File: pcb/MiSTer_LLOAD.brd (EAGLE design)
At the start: 100 x 80 mm, 22 parts, among them K1 692121030100

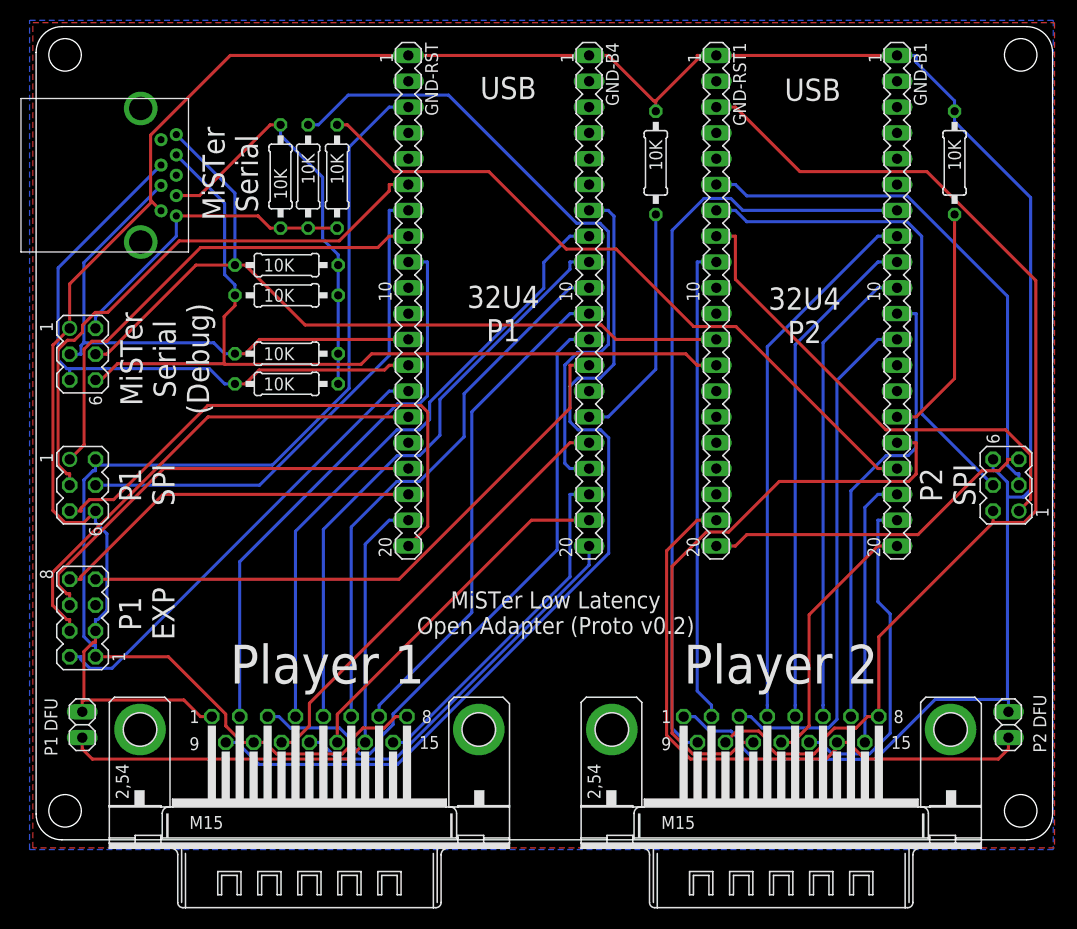
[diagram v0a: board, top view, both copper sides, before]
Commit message: Proto v0.3 PCB - It does not rely on Serial IO VCC anymore
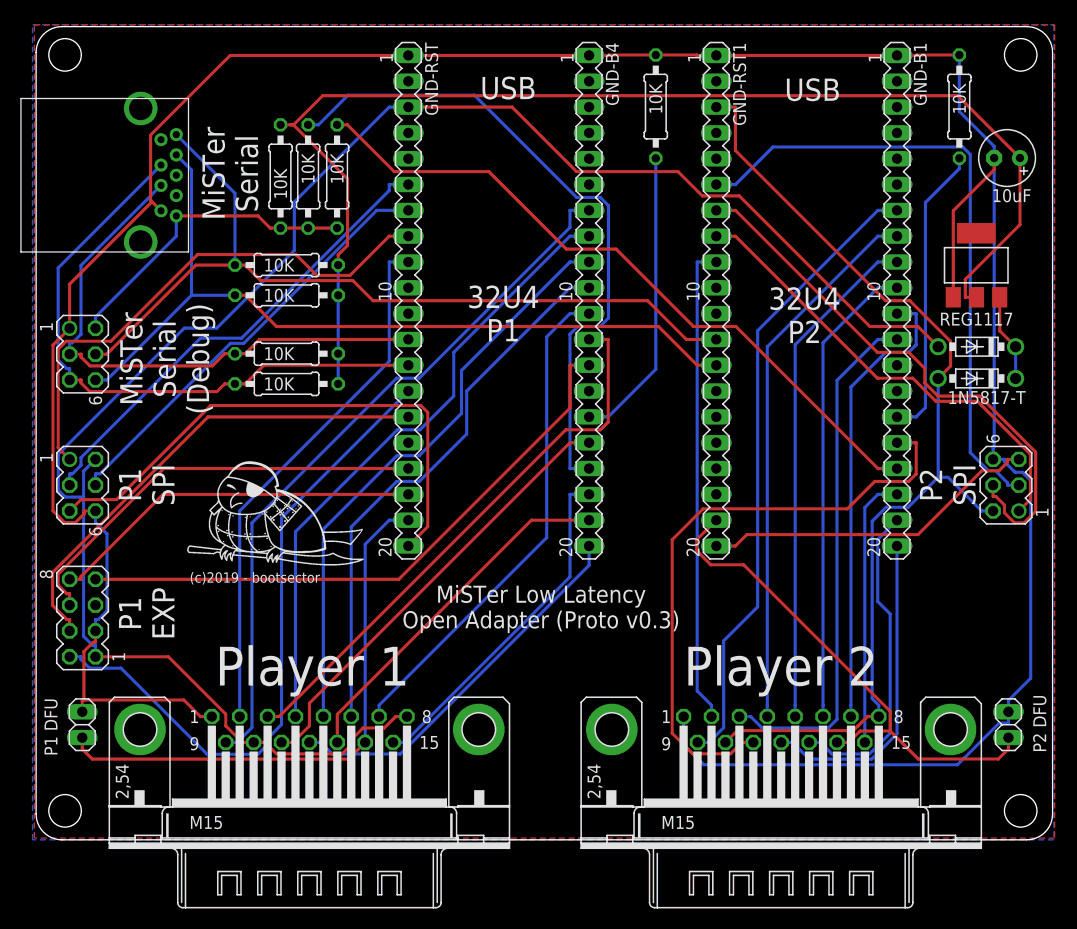
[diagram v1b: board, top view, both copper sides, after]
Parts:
- added C5: 10uF, rcl:E2,5-6
- added D1, D2: 1N5817-T, diode:DO41-7.6
- added IC3: REG1117, burr-brown:SOT223
- moved R4 5.55 mm to (90.8, 72.1)
- moved R1 5.53 mm to (61.0, 72.1)
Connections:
- new net VCC: D1.C, D2.C, IC3.3
- net 3V3: now also C5.+, IC3.2; no longer K1.6
- net GND: now also C5.-, IC3.1
- net P1_VCC: now also D1.A
- net P2_VCC: now also D2.A
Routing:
- net 3V3: track 41.0 -> 121.6 mm
- net P1_VCC: track 117.0 -> 177.2 mm
- net D2: track 45.2 -> 64.5 mm
- net E6: track 89.0 -> 70.2 mm
- net P2_E6: track 76.0 -> 62.2 mm
- net P2_D7: track 62.3 -> 51.3 mm
- net GND: track 277.7 -> 288.7 mm
- net P2_B1: track 52.4 -> 62.4 mm
- net P2_VCC: track 109.3 -> 99.7 mm
- net B1: track 55.9 -> 47.0 mm
- net VCC: track 0.00 -> 8.64 mm
- net B2: track 50.3 -> 42.6 mm
- net F6: track 62.7 -> 55.5 mm
- net P2_B2: track 48.7 -> 55.2 mm
- net P2_B4: track 25.8 -> 31.6 mm
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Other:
- board text added: "(c)2019 - bootsector"
- board text added: "MiSTer Low Latency Open Adapter (Proto v0.3)"
- board text removed: "MiSTer Low Latency Open Adapter (Proto v0.2)"

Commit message: Promoting LLOAD PCB to v1.0
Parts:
- removed SV2: (no value), con-lstb:MA04-2
- removed SV4: (no value), con-lstb:MA03-2
- moved R7 19.3 mm to (21.5, 46.1), turned to 270 degrees
- moved R8 19.3 mm to (24.2, 46.1), turned to 90 degrees
- moved R9 19.3 mm to (27.1, 46.1), turned to 90 degrees
- moved R2 15.9 mm to (9.39, 43.2)
- moved R3 15.9 mm to (9.39, 40.2)
- moved R5 15.9 mm to (9.39, 51.9)
- moved R6 15.9 mm to (9.39, 49.0)
- moved SV1 12.3 mm to (4.57, 22.6)
- moved SV3 12.3 mm to (95.4, 22.6)
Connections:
- net 3V3: now also X1.10, X2.10
- net D0: no longer SV4.3
- net D1: no longer SV4.5
- net D2: no longer SV2.2
- net D3: no longer SV2.4
- net D5: no longer SV2.6
- net D6: no longer SV2.8
- net F7: no longer SV2.7
- net GND: no longer SV2.3, SV4.1
- net LL_ENABLE: no longer SV4.2
- net P1_VCC: no longer SV2.1, X2.10
- net P2_D0: no longer SV4.4
- net P2_D1: no longer SV4.6
- net P2_VCC: no longer X1.10
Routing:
- net 3V3: track 121.6 -> 193.2 mm
- net D2: track 64.5 -> 0.00 mm
- net F7: track 59.8 -> 0.00 mm
- net D3: track 47.9 -> 0.00 mm
- net D5: track 42.4 -> 0.00 mm
- net D6: track 36.9 -> 0.00 mm
- net C6: track 65.9 -> 33.0 mm
- net F6: track 55.5 -> 83.5 mm
- net P2_C7: track 60.0 -> 39.9 mm
- net P2_VCC: track 99.7 -> 81.4 mm
- net P1_VCC: track 177.2 -> 161.6 mm
- net RST: track 53.7 -> 39.6 mm
- net GND: track 288.7 -> 276.0 mm
- net LL_ENABLE: track 30.7 -> 18.9 mm
- net B1: track 47.0 -> 57.9 mm
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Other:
- board text added: "LLOAD - Low Latency Open Adapter for MiSTer FPGA v1.0"
- board text removed: "MiSTer Low Latency Open Adapter (Proto v0.3)"
- board text removed: "MiSTer Serial (Debug)"
- board text removed: "P1 EXP"

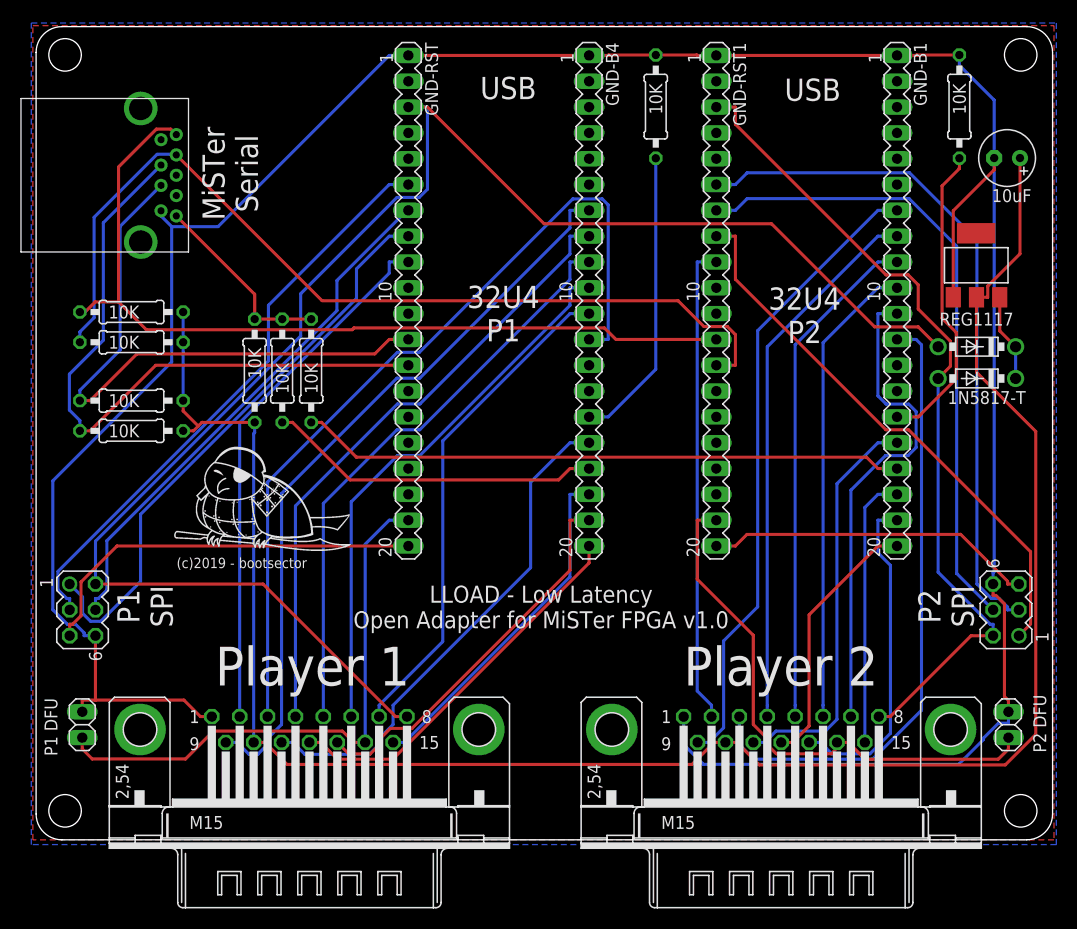
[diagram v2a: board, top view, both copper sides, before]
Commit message: Removed alternate VCC (3.3v) from DB15 pin 10. This will not make it directly compatible with supergun input, but at least no harm will be done in case someone inadvertently uses a supergun with it. Neo Geo and Neo Geo CD are still welcome in both revisions.
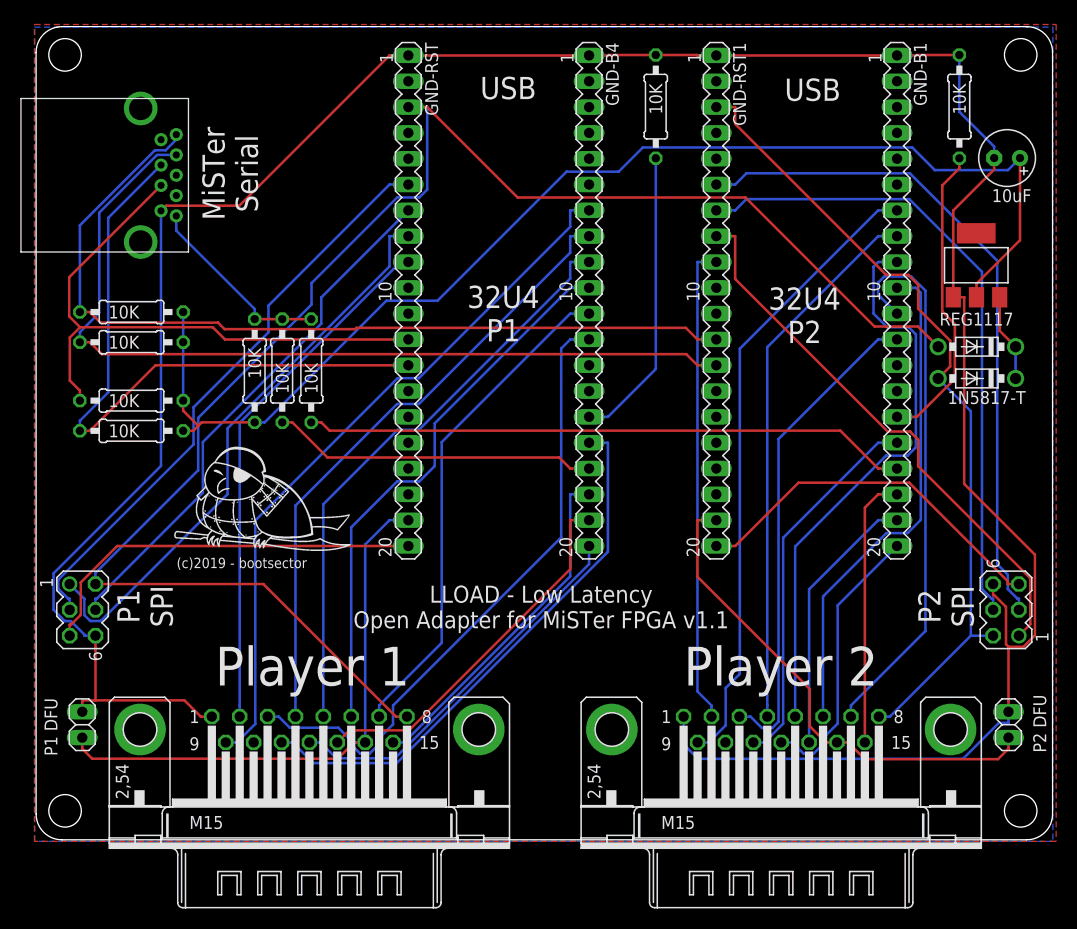
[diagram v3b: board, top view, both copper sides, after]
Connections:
- net 3V3: no longer X1.10, X2.10
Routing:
- net 3V3: track 193.2 -> 122.6 mm
- net F6: track 83.5 -> 62.6 mm
- net P2_F6: track 61.8 -> 48.1 mm
- net P2_B5: track 32.7 -> 26.5 mm
- net P2_F1: track 50.0 -> 55.9 mm
- net P2_F5: track 48.3 -> 54.2 mm
- net P2_D7: track 54.2 -> 49.1 mm
- net C7: track 49.8 -> 54.1 mm
- net P2_RST: track 32.4 -> 36.6 mm
- net P2_D1: track 90.8 -> 87.0 mm
- net P2_F4: track 46.3 -> 49.4 mm
- net GND: track 276.0 -> 273.0 mm
- net E6: track 73.0 -> 70.1 mm
- net P2_C7: track 39.9 -> 37.1 mm
- net P2_B4: track 25.8 -> 27.5 mm
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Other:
- board text added: "LLOAD - Low Latency Open Adapter for MiSTer FPGA v1.1"
- board text removed: "LLOAD - Low Latency Open Adapter for MiSTer FPGA v1.0"
